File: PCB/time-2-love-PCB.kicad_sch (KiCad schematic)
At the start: 0 parts

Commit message: Decided on an ESP 32 C3 WROOM 02 as mcu
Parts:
- added P1: USB_C_Plug_USB2.0, symbol Connector:USB_C_Plug_USB2.0
- added U1: ESP32-C3-WROOM-02, RF_Module:ESP32-C3-WROOM-02, symbol RF_Module:ESP32-C3-WROOM-02
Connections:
- new net: P1.A1 (GND), P1.A12 (GND), P1.B1 (GND), P1.B12 (GND)
- new net: P1.A4 (VBUS), P1.A9 (VBUS), P1.B4 (VBUS), P1.B9 (VBUS)
- new net: U1.19 (GND), U1.9 (GND)
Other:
- title: (none) -> Time2Love PCB
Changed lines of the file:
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@@
 	(generator_version "9.0")
 	(paper "A4")
+	(title_block
+		(title "Time2Love PCB")
+		(date "2025-12-16")
+		(rev "0.0.1")
+	)
+	(symbol
+		(lib_id "Connector:USB_C_Plug_USB2.0")
+		(at 124.46 54.61 0)
+		(unit 1)
+		(exclude_from_sim no)
+		(in_bom yes)
+		(on_board yes)
+		(dnp no)
+		(fields_autoplaced yes)
+		(property "Reference" "P1"
+			(at 124.46 31.75 0)
+			(effects
+				(font
+					(size 1.27 1.27)
+				)
+			)
+		)
+		(property "Value" "USB_C_Plug_USB2.0"
+			(at 124.46 34.29 0)
+			(effects
+				(font
+					(size 1.27 1.27)
+				)
+			)
+		)
+		(property "Footprint" ""
+			(at 128.27 54.61 0)
+			(effects
+				(font
+					(size 1.27 1.27)
+				)
+				(hide yes)
+			)
+		)
+		(property "Datasheet" "https://www.usb.org/sites/default/files/documents/usb_type-c.zip"
+			(at 128.27 54.61 0)
+			(effects
+				(font
+					(size 1.27 1.27)
+				)
+				(hide yes)
+			)
+		)
+		(property "Description" "USB 2.0-only Type-C Plug connector"
+			(at 124.46 54.61 0)
+			(effects
+				(font
+					(size 1.27 1.27)
+				)
+				(hide yes)
+			)
+		)
+		(pin "A6"
+		)
+		(pin "A7"
+		)
+		(pin "B5"
+		)
+		(pin "A5"
+		)
+		(pin "B9"
+		)
+		(pin "B4"
+		)
+		(pin "A9"
+		)
+		(pin "A4"
+		)
+		(pin "B12"
+		)
+		(pin "B1"
+		)
+		(pin "A12"
+		)
+		(pin "A1"
+		)
+		(pin "S1"
+		)
+		(instances
+			(project ""
+				(path "/5efd2621-235e-4aaf-8a47-7c4b2aa7d49b"
+					(reference "P1")
+					(unit 1)
+				)
+			)
+		)
+	)
+	(symbol
+		(lib_id "RF_Module:ESP32-C3-WROOM-02")
+		(at 52.07 55.88 0)
+		(unit 1)
+		(exclude_from_sim no)
+		(in_bom yes)
+		(on_board yes)
+		(dnp no)
+		(fields_autoplaced yes)
+		(property "Reference" "U1"
+			(at 54.2133 30.48 0)
+			(effects
+				(font
+					(size 1.27 1.27)
+				)
+				(justify left)
+			)
+		)
+		(property "Value" "ESP32-C3-WROOM-02"
+			(at 54.2133 33.02 0)
+			(effects
+				(font
+					(size 1.27 1.27)
+				)
+				(justify left)
+			)
+		)
+		(property "Footprint" "RF_Module:ESP32-C3-WROOM-02"
+			(at 52.07 55.245 0)
+			(effects
+				(font
+					(size 1.27 1.27)
+				)
+				(hide yes)
+			)
+		)
+		(property "Datasheet" "https://www.espressif.com/sites/default/files/documentation/esp32-c3-wroom-02_datasheet_en.pdf"
+			(at 52.07 55.245 0)
+			(effects
+				(font
+					(size 1.27 1.27)
+				)
+				(hide yes)
+			)
+		)
+		(property "Description" "802.11 b/g/n Wi­Fi and Bluetooth 5 module, ESP32­C3 SoC, RISC­V microprocessor, On-board antenna"
+			(at 52.07 55.245 0)
+			(effects
+				(font
+					(size 1.27 1.27)
+				)
+				(hide yes)
+			)
+		)
+		(pin "17"
+		)
+		(pin "16"
+		)
+		(pin "15"
+		)
+		(pin "12"
+		)
+		(pin "11"
+		)
+		(pin "9"
+		)
+		(pin "19"
+		)
+		(pin "1"
+		)
+		(pin "14"
+		)
+		(pin "13"
+		)
+		(pin "10"
+		)
+		(pin "8"
+		)
+		(pin "7"
+		)
+		(pin "6"
+		)
+		(pin "5"
+		)
+		(pin "4"
+		)
+		(pin "18"
+		)
+		(pin "2"
+		)
+		(pin "3"
+		)
+		(instances
+			(project ""
+				(path "/5efd2621-235e-4aaf-8a47-7c4b2aa7d49b"
+					(reference "U1")
+					(unit 1)
+				)
+			)
+		)
+	)
 	(sheet_instances
 		(path "/"

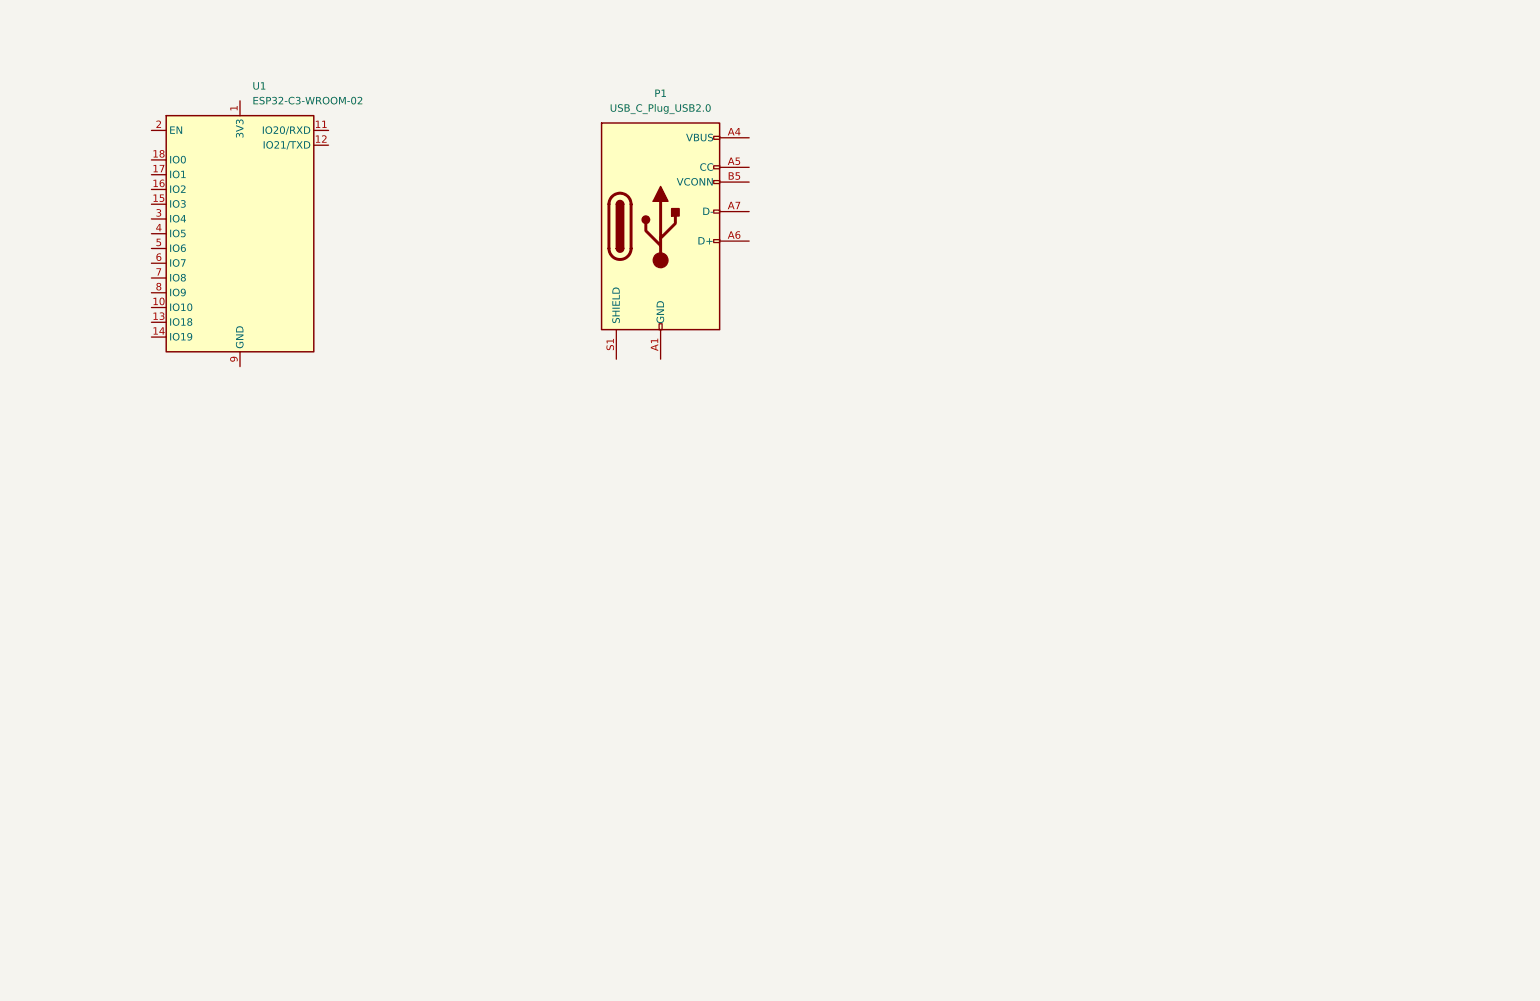
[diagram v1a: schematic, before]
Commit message: Added some components to the scematic
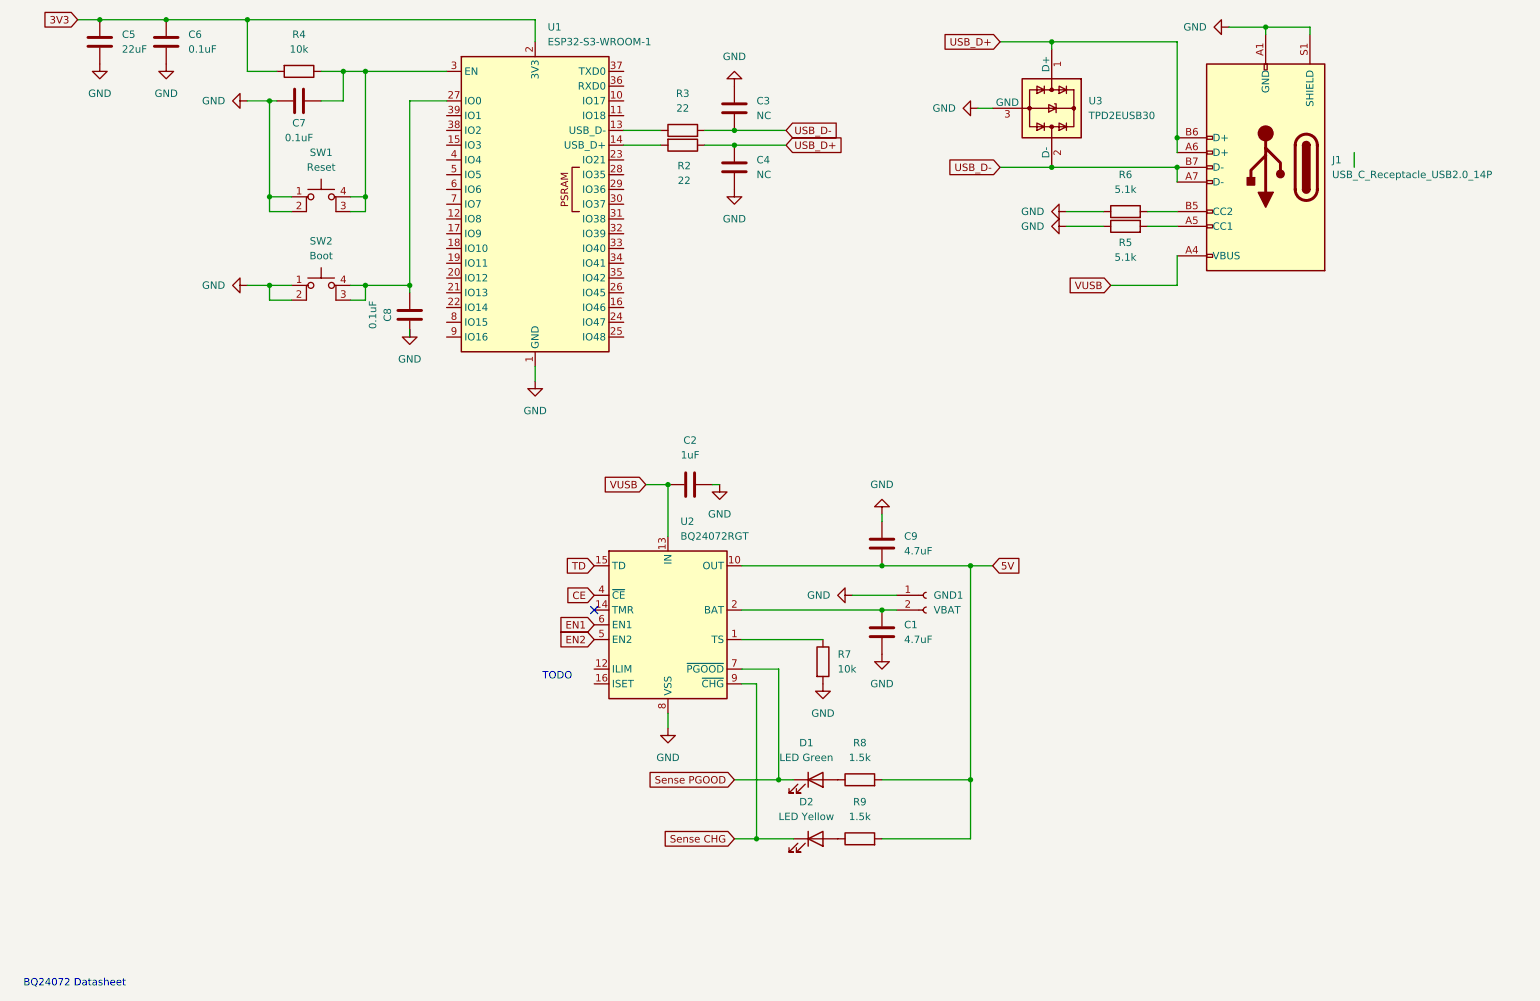
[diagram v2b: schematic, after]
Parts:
- removed P1: USB_C_Plug_USB2.0, symbol Connector:USB_C_Plug_USB2.0
- removed U1: ESP32-C3-WROOM-02, RF_Module:ESP32-C3-WROOM-02, symbol RF_Module:ESP32-C3-WROOM-02
- added C1, C9: 4.7uF, Capacitor_SMD:C_0603_1608Metric, symbol Device:C
- added C2: 1uF, Capacitor_SMD:C_0603_1608Metric, symbol Device:C
- added C3, C4: NC, Capacitor_SMD:C_0603_1608Metric, symbol Device:C
- added C5: 22uF, Capacitor_SMD:C_0603_1608Metric, symbol Device:C
- added C6, C7, C8: 0.1uF, Capacitor_SMD:C_0603_1608Metric, symbol Device:C
- added D1: LED Green, LED_SMD:LED_0603_1608Metric, symbol Device:LED
- added D2: LED Yellow, LED_SMD:LED_0603_1608Metric, symbol Device:LED
- added GND1: VBAT, Connector_JST:JST_PH_S2B-PH-K_1x02_P2.00mm_Horizontal, symbol Connector:Conn_01x02_Socket
- added J1: USB_C_Receptacle_USB2.0_14P, symbol Connector:USB_C_Receptacle_USB2.0_14P
- added R2, R3: 22, Resistor_SMD:R_0603_1608Metric, symbol Device:R
- added R4, R7: 10k, Resistor_SMD:R_0603_1608Metric, symbol Device:R
- added R5, R6: 5.1k, Resistor_SMD:R_0603_1608Metric, symbol Device:R
- added R8, R9: 1.5k, Resistor_SMD:R_0603_1608Metric, symbol Device:R
- added SW1: Reset, Button_Switch_SMD:SW_MEC_5GSH9, symbol Switch:SW_MEC_5E
- added SW2: Boot, Button_Switch_SMD:SW_MEC_5GSH9, symbol Switch:SW_MEC_5E
- added U1: ESP32-S3-WROOM-1, RF_Module:ESP32-S3-WROOM-1, symbol RF_Module:ESP32-S3-WROOM-1
- added U2: BQ24072RGT, Package_DFN_QFN:VQFN-16-1EP_3x3mm_P0.5mm_EP1.6x1.6mm, symbol Battery_Management:BQ24072RGT
- added U3: TPD2EUSB30, Package_TO_SOT_SMD:Texas_DRT-3, symbol Power_Protection:TPD2EUSB30
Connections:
- new net: R2.2, U1.14 (USB_D+)
- new net: C8.2, SW2.3 (K), SW2.4 (A), U1.27 (IO0)
- new net: C7.1, R4.1, SW1.3 (K), SW1.4 (A), U1.3 (EN)
- new net: D1.2 (A), R8.1
- new net: C1.1, GND1.2 (Pin_2), U2.2 (BAT), U2.3 (BAT)
- new net: R7.1, U2.1 (TS)
- new net: D2.2 (A), R9.1
- new net: J1.B5 (CC2), R6.2
- new net: J1.A5 (CC1), R5.2
- new net: R3.1, U1.13 (USB_D-)
- new net 3V3: C5.2, C6.2, R4.2, U1.2 (3V3)
- new net 5V: C9.2, R8.2, R9.2, U2.10 (OUT), U2.11 (OUT)
- new net CE: U2.4 (~{CE})
- new net EN1: U2.6 (EN1)
- new net EN2: U2.5 (EN2)
- new net GND: C1.2, C2.2, C3.2, C4.1, C5.1, C6.1, C7.2, C8.1, C9.1, GND1.1 (Pin_1), J1.A1 (GND), J1.A12 (GND), J1.B1 (GND), J1.B12 (GND), J1.S1 (SHIELD), R5.1, R6.1, R7.2, SW1.1, SW1.2, SW2.1, SW2.2, U1.1 (GND), U1.40 (GND), U1.41 (GND), U2.17 (VSS), U2.8 (VSS), U3.3 (GND)
- new net Sense CHG: D2.1 (K), U2.9 (~{CHG})
- new net Sense PGOOD: D1.1 (K), U2.7 (~{PGOOD})
- new net TD: U2.15 (TD)
- new net USB_D+: C4.2, J1.A6 (D+), J1.B6 (D+), R2.1, U3.1 (D+)
- new net USB_D-: C3.1, J1.A7 (D-), J1.B7 (D-), R3.2, U3.2 (D-)
- new net VUSB: C2.1, J1.A4 (VBUS), J1.A9 (VBUS), J1.B4 (VBUS), J1.B9 (VBUS), U2.13 (IN)
- no-connect marks 0 -> 1
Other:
- note added: "BQ24072 Datasheet"
- note added: "TODO"
